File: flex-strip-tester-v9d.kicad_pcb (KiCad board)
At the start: 2 copper layers, 68.8 x 11.1 mm, 11 parts, among them J2 Conn_01x01_Female

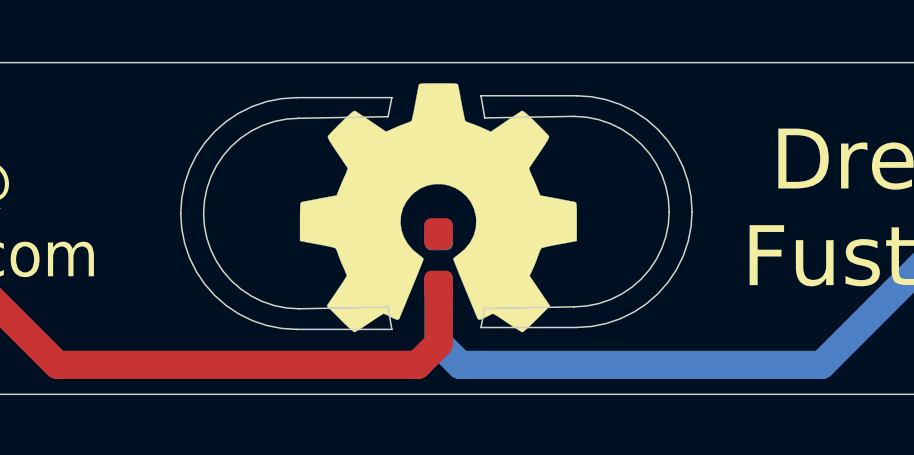
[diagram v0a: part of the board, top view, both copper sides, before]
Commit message: rework cutout and add oshw logo to center
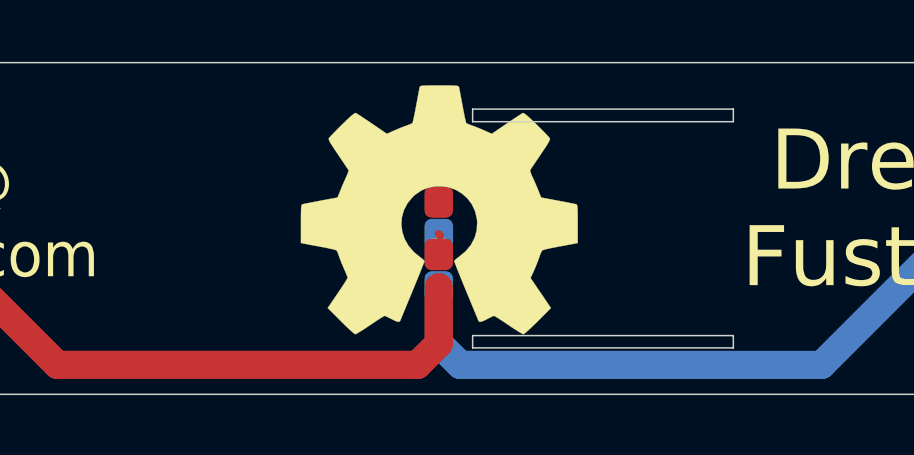
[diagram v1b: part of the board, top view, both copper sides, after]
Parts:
- moved D1 1.07 mm to (153.2, 95.8)
- moved J2 0.08 mm to (153.2, 96.5)
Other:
- outline, holes or cut-outs redrawn
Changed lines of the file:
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@@
   (general
     (thickness 0.1)
-    (drawings 54)
+    (drawings 57)
     (tracks 15)
     (modules 11)
@@
   (paper "A4")
   (layers
-    (0 "F.Cu" signal hide)
-    (31 "B.Cu" signal hide)
-    (32 "B.Adhes" user hide)
-    (33 "F.Adhes" user hide)
-    (34 "B.Paste" user hide)
-    (35 "F.Paste" user hide)
-    (36 "B.SilkS" user hide)
+    (0 "F.Cu" signal)
+    (31 "B.Cu" signal)
+    (32 "B.Adhes" user)
+    (33 "F.Adhes" user)
+    (34 "B.Paste" user)
+    (35 "F.Paste" user)
+    (36 "B.SilkS" user)
     (37 "F.SilkS" user)
-    (38 "B.Mask" user hide)
-    (39 "F.Mask" user hide)
-    (40 "Dwgs.User" user hide)
-    (41 "Cmts.User" user hide)
-    (42 "Eco1.User" user hide)
-    (43 "Eco2.User" user hide)
+    (38 "B.Mask" user)
+    (39 "F.Mask" user)
+    (40 "Dwgs.User" user)
+    (41 "Cmts.User" user)
+    (42 "Eco1.User" user)
+    (43 "Eco2.User" user)
     (44 "Edge.Cuts" user)
-    (45 "Margin" user hide)
-    (46 "B.CrtYd" user hide)
-    (47 "F.CrtYd" user hide)
-    (48 "B.Fab" user hide)
-    (49 "F.Fab" user hide)
+    (45 "Margin" user)
+    (46 "B.CrtYd" user)
+    (47 "F.CrtYd" user)
+    (48 "B.Fab" user)
+    (49 "F.Fab" user)
   )
   (setup
@@
   )
   (module "afterdark:OSHW-Logo2_14.6x12mm_Copper" (layer "F.Cu")
-    (at 153.19 96.47)
+    (at 153.22 96.54)
     (descr "Open Source Hardware Symbol")
     (tags "Logo Symbol OSHW")
@@
   )
   (module "LED_SMD:LED_0603_1608Metric_Pad1.05x0.95mm_HandSolder" (layer "F.Cu")
-    (at 153.19 96.815 90)
+    (at 153.2 95.75 90)
     (descr "LED SMD 0603 (1608 Metric), square (rectangular) end terminal, IPC_7351 nominal, (Body size source: http://www.tortai-tech.com/upload/download/2011102023233369053.pdf), generated with kicad-footprint-generator")
     (tags "LED handsolder")
@@
     )
   )
+  (gr_line (start 154.33 99.33) (end 154.33 99.74) (layer "Edge.Cuts") (width 0.05))
+  (gr_line (start 163.02 99.33) (end 163.02 99.74) (layer "Edge.Cuts") (width 0.05))
+  (gr_line (start 163.02 91.78) (end 163.02 92.2) (layer "Edge.Cuts") (width 0.05))
+  (gr_line (start 154.33 91.78) (end 154.33 92.2) (layer "Edge.Cuts") (width 0.05))
+  (gr_line (start 154.33 92.2) (end 163.02 92.2) (layer "Edge.Cuts") (width 0.05))
+  (gr_line (start 154.33 91.78) (end 163.02 91.78) (layer "Edge.Cuts") (width 0.05))
+  (gr_line (start 154.33 99.74) (end 163.02 99.74) (layer "Edge.Cuts") (width 0.05))
+  (gr_line (start 154.33 99.33) (end 163.02 99.33) (layer "Edge.Cuts") (width 0.05))
+  (gr_line (start 158.93 91.83) (end 158.93 92.15) (layer "Eco2.User") (width 0.0508))
+  (gr_line (start 158.93 90.28) (end 158.93 91.73) (layer "Eco2.User") (width 0.0508))
+  (gr_line (start 158.93 99.79) (end 158.93 101.24) (layer "Eco2.User") (width 0.0508))
+  (gr_line (start 158.93 99.37) (end 158.93 99.69) (layer "Eco2.User") (width 0.0508))
+  (gr_line (start 153.15 90.94) (end 152.31 90.94) (layer "Cmts.User") (width 0.0508))
+  (gr_line (start 154.09 90.94) (end 153.25 90.94) (layer "Cmts.User") (width 0.0508))
+  (gr_line (start 154.14 90.89) (end 154.14 92.42) (layer "Eco2.User") (width 0.0508))
+  (gr_line (start 152.32 90.89) (end 154.14 90.89) (layer "Eco2.User") (width 0.0508))
+  (gr_line (start 152.32 92.43) (end 152.32 90.89) (layer "Eco2.User") (width 0.0508))
+  (gr_line (start 113.95 95.76) (end 153.2 95.76) (layer "Eco2.User") (width 0.0508))
+  (gr_line (start 153.2 95.76) (end 192.45 95.76) (layer "Eco2.User") (width 0.0508))
+  (gr_line (start 153.2 95.76) (end 153.2 90.28) (layer "Eco2.User") (width 0.0508))
+  (gr_line (start 163.1 102.475) (end 163.1 88.925) (layer "Eco2.User") (width 0.1))
+  (gr_line (start 142.175 102.625) (end 142.175 89.075) (layer "Eco2.User") (width 0.1))
+  (gr_line (start 153.2 100.625) (end 117.4 100.625) (layer "Margin") (width 0.0508))
+  (gr_line (start 153.2 100.625) (end 189 100.625) (layer "Margin") (width 0.0508))
+  (gr_line (start 153.2 101.235) (end 153.2 100.625) (layer "Margin") (width 0.0508))
+  (gr_line (start 153.2 100.625) (end 153.2 90.89) (layer "Margin") (width 0.0508))
+  (gr_line (start 117.4 90.89) (end 153.2 90.89) (layer "Margin") (width 0.0508))
+  (gr_line (start 153.2 90.89) (end 189 90.89) (layer "Margin") (width 0.0508))
+  (gr_line (start 153.2 90.89) (end 153.2 90.28) (layer "Margin") (width 0.0508))
   (gr_line (start 188.97 90.8) (end 94.33468 90.8) (layer "Eco1.User") (width 0.15))
   (gr_line (start 118.89 95.43) (end 153.23 95.43) (layer "B.Fab") (width 0.1))
-  (gr_line (start 151.7015 92.075) (end 151.7015 98.425) (layer "Eco2.User") (width 0.1))
   (gr_line (start 184.72404 90.23096) (end 186.25714 90.238094) (layer "Edge.Cuts") (width 0.05))
   (gr_line (start 184.70118 101.28758) (end 186.28 101.294714) (layer "Edge.Cuts") (width 0.05))
@@
     (effects (font (size 2 2) (thickness 0.3)))
   )
-  (gr_line (start 151.638 99.1235) (end 148.463 99.1235) (layer "Edge.Cuts") (width 0.05))
-  (gr_line (start 151.638 99.1235) (end 151.511 98.383392) (layer "Edge.Cuts") (width 0.05))
-  (gr_line (start 151.511 98.383392) (end 148.537446 98.435946) (layer "Edge.Cuts") (width 0.05))
   (gr_line (start 151.7015 98.425) (end 151.7015 99.06) (layer "Eco1.User") (width 0.1))
   (gr_line (start 152.347446 99.1235) (end 151.648946 99.1235) (layer "Eco1.User") (width 0.1))
   (gr_line (start 155.2575 99.06) (end 154.6225 99.06) (layer "Eco1.User") (width 0.1))
-  (gr_line (start 156.220946 98.4885) (end 133.233946 98.4885) (layer "Eco2.User") (width 0.1))
-  (gr_arc (start 148.463 95.260946) (end 144.600446 95.260946) (angle -90) (layer "Edge.Cuts") (width 0.05))
-  (gr_line (start 151.511 92.033392) (end 151.638 91.398392) (layer "Edge.Cuts") (width 0.05))
-  (gr_arc (start 148.537446 95.260946) (end 145.362446 95.260946) (angle -90) (layer "Edge.Cuts") (width 0.05))
-  (gr_line (start 148.537446 92.085946) (end 151.511 92.033392) (layer "Edge.Cuts") (width 0.05))
-  (gr_arc (start 148.537446 95.260946) (end 148.537446 92.085946) (angle -90) (layer "Edge.Cuts") (width 0.05))
-  (gr_arc (start 148.463 95.260946) (end 148.463 91.398392) (angle -90) (layer "Edge.Cuts") (width 0.05))
-  (gr_line (start 151.638 91.398392) (end 148.463 91.398392) (layer "Edge.Cuts") (width 0.05))
   (gr_line (start 154.6225 99.06) (end 154.6225 98.3615) (layer "Eco1.User") (width 0.1))
-  (gr_line (start 154.607169 91.334892) (end 154.734169 92.075) (layer "Edge.Cuts") (width 0.05))
-  (gr_line (start 154.734169 92.075) (end 157.707723 92.022446) (layer "Edge.Cuts") (width 0.05))
-  (gr_line (start 154.607169 91.334892) (end 157.782169 91.334892) (layer "Edge.Cuts") (width 0.05))
-  (gr_line (start 154.607169 99.06) (end 157.782169 99.06) (layer "Edge.Cuts") (width 0.05))
-  (gr_line (start 154.734169 98.425) (end 154.607169 99.06) (layer "Edge.Cuts") (width 0.05))
-  (gr_line (start 157.707723 98.372446) (end 154.734169 98.425) (layer "Edge.Cuts") (width 0.05))
-  (gr_line (start 154.6225 92.0115) (end 154.6225 98.3615) (layer "Eco2.User") (width 0.1))
-  (gr_line (start 156.220946 99.1235) (end 133.233946 99.1235) (layer "Eco2.User") (width 0.1))
-  (gr_line (start 156.220946 92.1385) (end 133.233946 92.1385) (layer "Eco2.User") (width 0.1))
-  (gr_line (start 156.220946 91.44) (end 133.233946 91.44) (layer "Eco2.User") (width 0.1))
-  (gr_arc (start 157.782169 95.197446) (end 161.644723 95.197446) (angle -90) (layer "Edge.Cuts") (width 0.05))
-  (gr_arc (start 157.707723 95.197446) (end 157.707723 98.372446) (angle -90) (layer "Edge.Cuts") (width 0.05))
-  (gr_arc (start 157.782169 95.197446) (end 157.782169 99.06) (angle -90) (layer "Edge.Cuts") (width 0.05))
-  (gr_arc (start 157.707723 95.197446) (end 160.882723 95.197446) (angle -90) (layer "Edge.Cuts") (width 0.05))
   (gr_text "drew@\noshpark.com" (at 135.66902 95.45066) (layer "F.SilkS")
     (effects (font (size 1.5 1.4) (thickness 0.2)))
@@
   (segment (start 140.4874 100.3046) (end 135.7122 95.5294) (width 0.9398) (layer "F.Cu") (net 1))
   (segment (start 135.7122 95.5294) (end 128.6002 95.5294) (width 0.9398) (layer "F.Cu") (net 1))
-  (segment (start 153.24386 95.99386) (end 153.19 95.94) (width 0.25) (layer "F.Cu") (net 2))
+  (segment (start 153.24386 95.99386) (end 153.19 95.94) (width 0.25) (layer "F.Cu") (net 1))
   (segment (start 165.96355 100.30635) (end 170.73875 95.53115) (width 0.9398) (layer "B.Cu") (net 2))
   (segment (start 170.75 95.53) (end 177.862 95.53) (width 0.9398) (layer "B.Cu") (net 2))

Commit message: update flextester
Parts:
- moved D1 0.81 mm to (153.2, 96.0)
- moved D1 0.28 mm to (153.2, 96.0)
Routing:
- net +3V3: track 28.8 -> 34.7 mm, vias 1 -> 2
- net GND: track 28.8 -> 34.6 mm, vias 1 -> 2
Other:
- outline, holes or cut-outs redrawn
